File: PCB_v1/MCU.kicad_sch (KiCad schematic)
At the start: 41 parts, among them J8 Conn_ARM_JTAG_SWD_10, J9 Conn_01x03, SW8 SW_Push, SW9 SW_SPDT, U6 STM32F405RGTx, Y1 Crystal

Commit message: adding the crystal
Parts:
- C15, C16, C17, C18, C19, C20, C21, C22, C23, C24, C25, C26, C27, C28, C29: symbol Device:C -> GT_LIbrary:C
- C30, C31: symbol Device:C_Polarized_US -> GT_LIbrary:C_Polarized_US
- D6, D7, D8, D9: symbol Device:LED -> GT_LIbrary:LED
- FB1: symbol Device:FerriteBead -> GT_LIbrary:FerriteBead
- J8: symbol Connector:Conn_ARM_JTAG_SWD_10 -> GT_LIbrary:Conn_ARM_JTAG_SWD_10
- J9: symbol Connector_Generic:Conn_01x03 -> GT_LIbrary:Conn_01x03
- R21, R22, R23: symbol Device:R_US -> GT_LIbrary:R_US
- RN3, RN4: symbol Device:R_Pack04_Split -> GT_LIbrary:R_Pack04_Split
- SW8: symbol Switch:SW_Push -> GT_LIbrary:SW_Push
- SW9: symbol Switch:SW_SPDT -> GT_LIbrary:SW_SPDT
- TP10, TP11, TP12, TP13, TP7, TP8, TP9: symbol Connector:TestPoint -> GT_LIbrary:TestPoint
- U6: symbol MCU_ST_STM32F4:STM32F405RGTx -> GT_LIbrary:STM32F405RGTx
- XTAL1: symbol MC306:MC-306_32.7680K-E3_ROHS -> GT_LIbrary:MC-306_32.7680K-E3_ROHS
- Y1: footprint (none) -> LFXTAL003237Bulk; symbol Device:Crystal -> GT_LIbrary:Crystal

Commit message: before oscilator
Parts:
- XTAL1: footprint Parts_Library:SO4_MC-306_SEC -> SO4_MC-306_SEC
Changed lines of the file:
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@@
 			)
 		)
-		(property "Footprint" "Parts_Library:SO4_MC-306_SEC"
+		(property "Footprint" "SO4_MC-306_SEC"
 			(at 64.77 203.2 0)
 			(effects

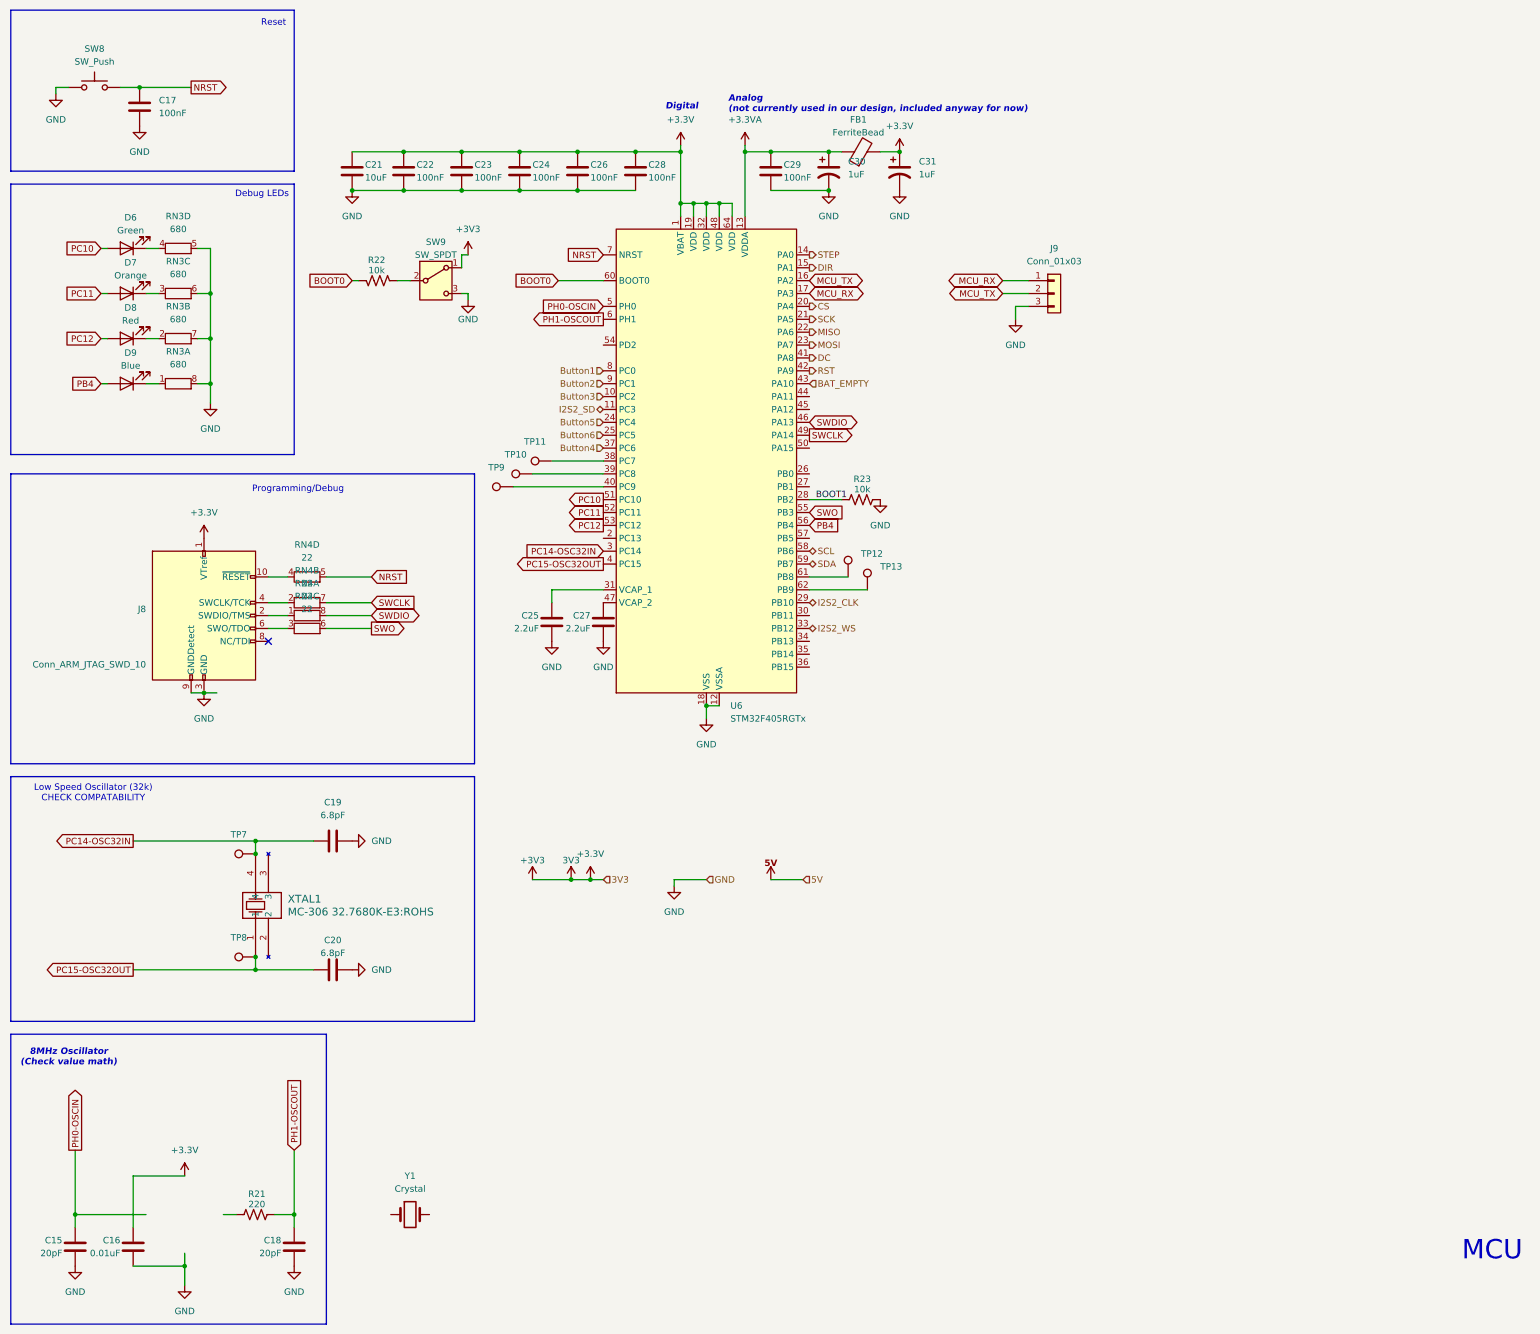
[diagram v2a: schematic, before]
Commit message: added the oscilator
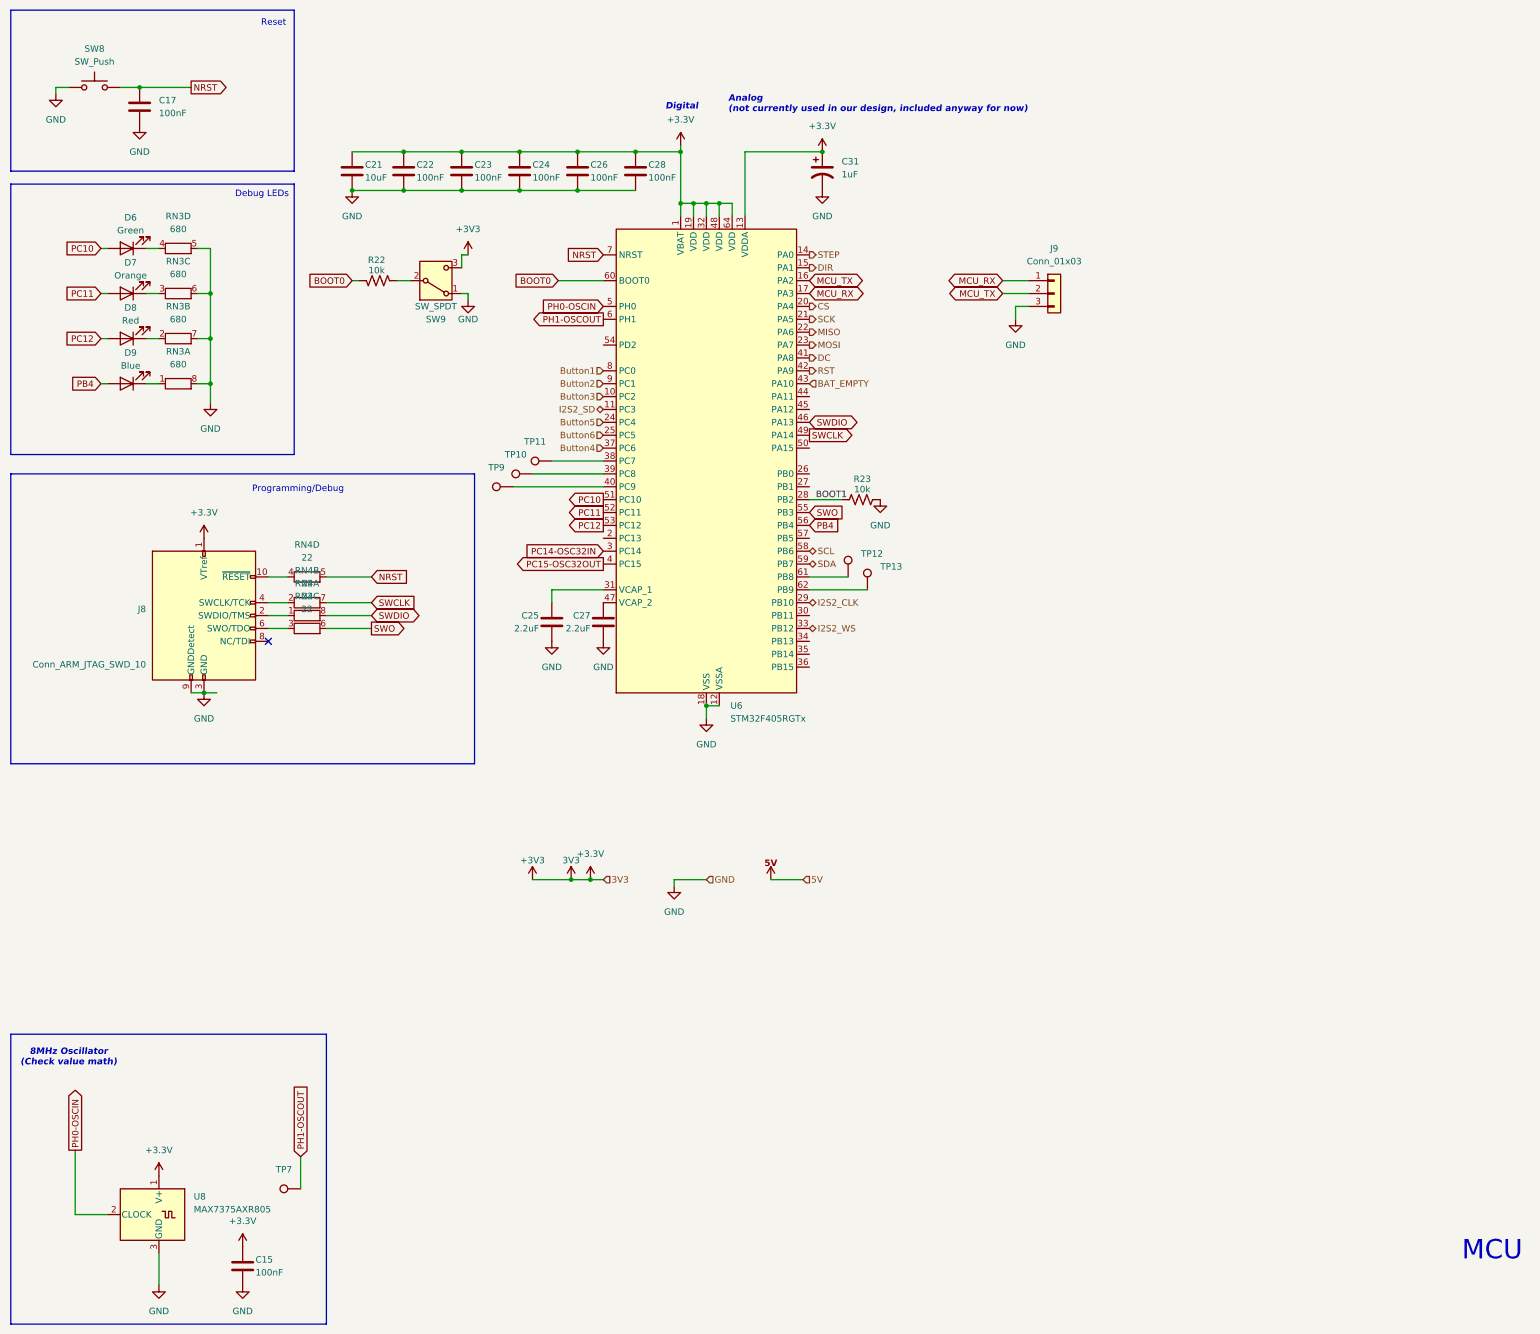
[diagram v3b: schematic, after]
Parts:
- removed C16: 0.01uF, Capacitor_SMD:C_0805_2012Metric, symbol GT_LIbrary:C
- removed C18: 20pF, Capacitor_SMD:C_0805_2012Metric, symbol GT_LIbrary:C
- removed C19, C20: 6.8pF, Capacitor_SMD:C_0805_2012Metric, symbol GT_LIbrary:C
- removed C29: 100nF, Capacitor_SMD:C_0805_2012Metric, symbol GT_LIbrary:C
- removed C30: 1uF, Capacitor_SMD:C_1206_3216Metric_Pad1.33x1.80mm_HandSolder, symbol GT_LIbrary:C_Polarized_US
- removed FB1: FerriteBead, Inductor_SMD:L_0603_1608Metric, symbol GT_LIbrary:FerriteBead
- removed R21: 220, Resistor_SMD:R_0805_2012Metric, symbol GT_LIbrary:R_US
- removed TP8: ~, TestPoint:TestPoint_THTPad_D1.0mm_Drill0.5mm, symbol GT_LIbrary:TestPoint
- removed XTAL1: MC-306 32.7680K-E3:ROHS, SO4_MC-306_SEC, symbol GT_LIbrary:MC-306_32.7680K-E3_ROHS
- removed Y1: Crystal, LFXTAL003237Bulk, symbol GT_LIbrary:Crystal
- added U8: MAX7375AXR805, Package_TO_SOT_SMD:SOT-323_SC-70, symbol Oscillator:MAX7375AXR805
- C15: value 20pF -> 100nF
- D6, D7, D8, D9: footprint LED_SMD:LED_0805_2012Metric_Pad1.15x1.40mm_HandSolder -> LED_0805_2012Metric_Pad1.15x1.40mm_HandSolder
- TP10, TP11, TP12, TP13, TP7, TP9: footprint TestPoint:TestPoint_THTPad_D1.0mm_Drill0.5mm -> TestPoint_THTPad_D0.5mm_Drill0.3mm
- U6: footprint Package_QFP:LQFP-64_10x10mm_P0.5mm -> LQFP-64_10x10mm_P0.5mm
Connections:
- net +3.3VA is gone; now on net +3.3V: U6.13 (VDDA)
- net +3.3V: now also C15.1, SW9.3 (C), U8.1 (V+); no longer SW9.1 (A)
- net GND: now also SW9.1 (A), U8.3 (GND); no longer SW9.3 (C)
- net PC14-OSC32IN: no longer TP7.1
- net PH0-OSCIN: now also U8.2 (CLOCK); no longer C15.1
- net PH1-OSCOUT: now also TP7.1
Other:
- note removed: "Low Speed Oscillator (32k) CHECK COMPATABILITY"
- moved on the sheet: C31

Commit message: push for jtag fix
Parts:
- J8: footprint Connector_PinHeader_2.54mm:PinHeader_2x05_P2.54mm_Vertical -> Connector_IDC:IDC-Header_2x05_P2.54mm_Vertical
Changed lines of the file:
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@@
 	(label "BOOT1"
 		(at 175.26 113.03 0)
-		(fields_autoplaced yes)
 		(effects
 			(font
@@
 		(shape bidirectional)
 		(at 173.99 138.43 0)
-		(fields_autoplaced yes)
 		(effects
 			(font
@@
 		(shape input)
 		(at 172.72 187.96 0)
-		(fields_autoplaced yes)
 		(effects
 			(font
@@
 		(shape output)
 		(at 173.99 80.01 0)
-		(fields_autoplaced yes)
 		(effects
 			(font
@@
 		(shape bidirectional)
 		(at 173.99 125.73 0)
-		(fields_autoplaced yes)
 		(effects
 			(font
@@
 		(shape output)
 		(at 173.99 85.09 0)
-		(fields_autoplaced yes)
 		(effects
 			(font
@@
 		(shape input)
 		(at 133.35 100.33 180)
-		(fields_autoplaced yes)
 		(effects
 			(font
@@
 		(shape input)
 		(at 173.99 90.17 0)
-		(fields_autoplaced yes)
 		(effects
 			(font
@@
 		(shape output)
 		(at 173.99 87.63 0)
-		(fields_autoplaced yes)
 		(effects
 			(font
@@
 		(shape input)
 		(at 133.35 92.71 180)
-		(fields_autoplaced yes)
 		(effects
 			(font
@@
 		(shape input)
 		(at 133.35 102.87 180)
-		(fields_autoplaced yes)
 		(effects
 			(font
@@
 		(shape input)
 		(at 133.35 97.79 180)
-		(fields_autoplaced yes)
 		(effects
 			(font
@@
 		(shape input)
 		(at 133.35 187.96 0)
-		(fields_autoplaced yes)
 		(effects
 			(font
@@
 		(shape input)
 		(at 133.35 90.17 180)
-		(fields_autoplaced yes)
 		(effects
 			(font
@@
 		(shape input)
 		(at 153.67 187.96 0)
-		(fields_autoplaced yes)
 		(effects
 			(font
@@
 		(shape output)
 		(at 173.99 74.93 0)
-		(fields_autoplaced yes)
 		(effects
 			(font
@@
 		(shape output)
 		(at 173.99 77.47 0)
-		(fields_autoplaced yes)
 		(effects
 			(font
@@
 		(shape output)
 		(at 173.99 64.77 0)
-		(fields_autoplaced yes)
 		(effects
 			(font
@@
 		(shape output)
 		(at 173.99 82.55 0)
-		(fields_autoplaced yes)
 		(effects
 			(font
@@
 		(shape bidirectional)
 		(at 133.35 95.25 180)
-		(fields_autoplaced yes)
 		(effects
 			(font
@@
 		(shape bidirectional)
 		(at 173.99 123.19 0)
-		(fields_autoplaced yes)
 		(effects
 			(font
@@
 		(shape input)
 		(at 133.35 87.63 180)
-		(fields_autoplaced yes)
 		(effects
 			(font
@@
 		(shape bidirectional)
 		(at 173.99 133.35 0)
-		(fields_autoplaced yes)
 		(effects
 			(font
@@
 		(shape output)
 		(at 173.99 67.31 0)
-		(fields_autoplaced yes)
 		(effects
 			(font
@@
 			)
 		)
-		(property "Footprint" "Connector_PinHeader_2.54mm:PinHeader_2x05_P2.54mm_Vertical"
+		(property "Footprint" "Connector_IDC:IDC-Header_2x05_P2.54mm_Vertical"
 			(at 52.832 140.462 0)
 			(effects

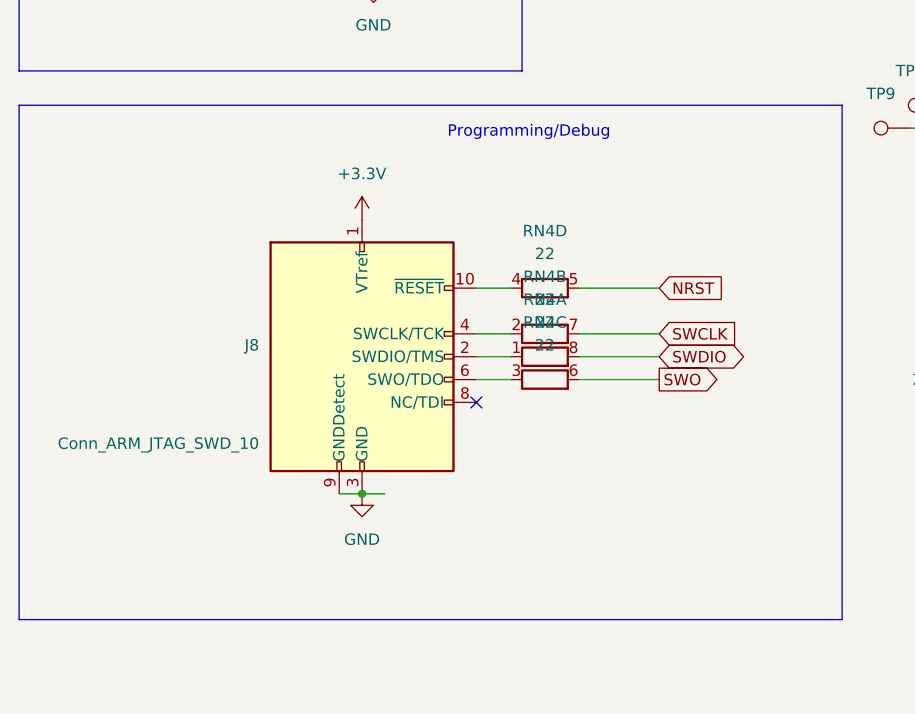
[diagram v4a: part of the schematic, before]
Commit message: Updated debug connection on MCU
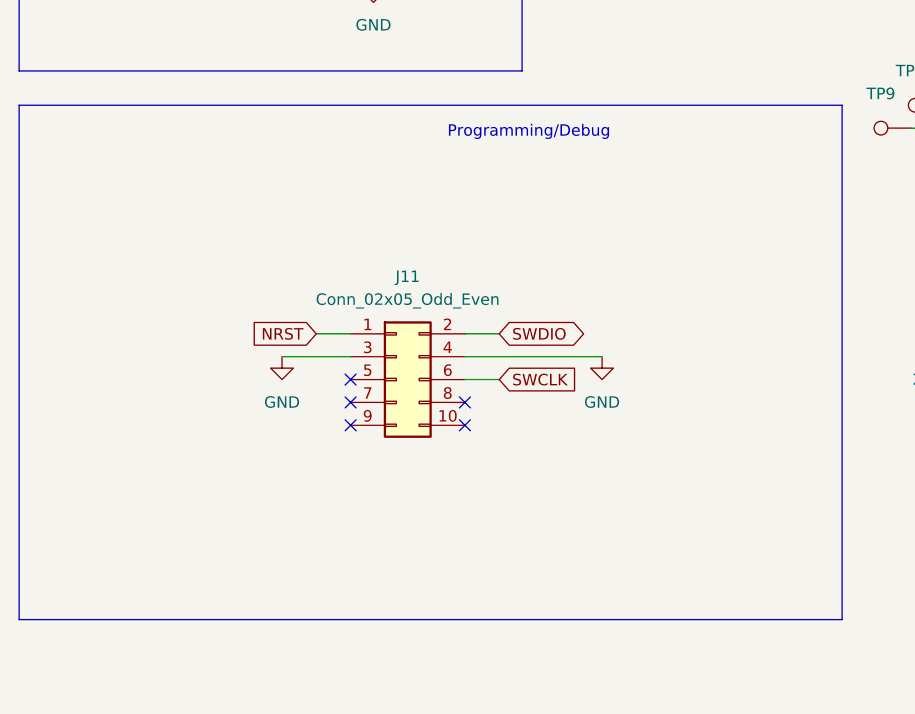
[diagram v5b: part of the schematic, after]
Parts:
- removed J8: Conn_ARM_JTAG_SWD_10, Connector_IDC:IDC-Header_2x05_P2.54mm_Vertical, symbol GT_LIbrary:Conn_ARM_JTAG_SWD_10
- removed RN4: 22, Parts_Library:RESCAXE80P320X160X70-8N, symbol GT_LIbrary:R_Pack04_Split
- added J11: Conn_02x05_Odd_Even, Connector_Harwin:Harwin_LTek-Male_2x05_P2.00mm_Vertical, symbol Connector_Generic:Conn_02x05_Odd_Even
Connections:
- net GND: now also J11.3 (Pin_3), J11.4 (Pin_4)
- net NRST: now also J11.1 (Pin_1)
- net SWCLK: now also J11.6 (Pin_6)
- net SWDIO: now also J11.2 (Pin_2)
- no-connect marks 1 -> 5

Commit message: before major move
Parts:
- added J8: Conn_01x02_Pin, Connector_PinHeader_2.54mm:PinHeader_1x02_P2.54mm_Vertical, symbol Connector:Conn_01x02_Pin
- added R23: 10k, Resistor_SMD:R_0805_2012Metric, symbol GT_LIbrary:R_US
- J9: renamed from J11; footprint Connector_Harwin:Harwin_LTek-Male_2x05_P2.00mm_Vertical -> Connector_IDC:IDC-Header_2x05_P2.54mm_Vertical
- TP10: renamed from TP11; footprint TestPoint_THTPad_D0.5mm_Drill0.3mm -> TestPoint_THTPad_D0.8mm_Drill0.4mm
- TP11: renamed from TP12; footprint TestPoint_THTPad_D0.5mm_Drill0.3mm -> TestPoint_THTPad_D0.8mm_Drill0.4mm
- TP12: renamed from TP13; footprint TestPoint_THTPad_D0.5mm_Drill0.3mm -> TestPoint_THTPad_D0.8mm_Drill0.4mm
- TP7: footprint TestPoint_THTPad_D0.5mm_Drill0.3mm -> TestPoint_THTPad_D0.8mm_Drill0.4mm
- TP8: renamed from TP9; footprint TestPoint_THTPad_D0.5mm_Drill0.3mm -> TestPoint_THTPad_D0.8mm_Drill0.4mm
- TP9: renamed from TP10; footprint TestPoint_THTPad_D0.5mm_Drill0.3mm -> TestPoint_THTPad_D0.8mm_Drill0.4mm
- renumbered C17 to C15, C15 to C16, C21 to C17, C22 to C18, C23 to C19, C24 to C20, C25 to C21, C26 to C22, C27 to C23, C28 to C24, C31 to C25, J9 to J10, R22 to R21, R23 to R22, U8 to U6, U6 to U7
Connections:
- net +3.3V: now also J8.1 (Pin_1), R23.1
- net NRST: now also R23.2
- net at J9.7 (Pin_7): now also J9.8 (Pin_8), J8.2 (Pin_2)
- no-connect marks 5 -> 3

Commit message: Placement done
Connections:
- net MCU_RX: now also J10.2 (Pin_2); no longer J10.1 (Pin_1)
- net MCU_TX: now also J10.1 (Pin_1); no longer J10.2 (Pin_2)
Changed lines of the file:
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@@
-	(wire
-		(pts
-			(xy 212.09 72.39) (xy 217.17 72.39)
-		)
-		(stroke
-			(width 0)
-			(type default)
-		)
-	)
 	(wire
 		(pts
@@
 	(wire
 		(pts
-			(xy 212.09 69.85) (xy 217.17 69.85)
-		)
-		(stroke
-			(width 0)
-			(type default)
-		)
-	)
-	(wire
-		(pts
 			(xy 173.99 130.81) (xy 185.42 130.81)
 		)
@@
 	(wire
 		(pts
+			(xy 214.63 72.39) (xy 217.17 72.39)
+		)
+		(stroke
+			(width 0)
+			(type default)
+		)
+	)
+	(wire
+		(pts
 			(xy 153.67 153.67) (xy 156.21 153.67)
 		)
@@
 	(wire
 		(pts
+			(xy 176.53 138.43) (xy 173.99 138.43)
+		)
+		(stroke
+			(width 0)
+			(type default)
+		)
+	)
+	(wire
+		(pts
 			(xy 69.85 146.05) (xy 49.53 146.05)
 		)
@@
 	(wire
 		(pts
+			(xy 214.63 69.85) (xy 217.17 69.85)
+		)
+		(stroke
+			(width 0)
+			(type default)
+		)
+	)
+	(wire
+		(pts
 			(xy 35.56 63.5) (xy 34.29 63.5)
 		)
@@
 		(pts
 			(xy 53.34 72.39) (xy 55.88 72.39)
+		)
+		(stroke
+			(width 0)
+			(type default)
+		)
+	)
+	(wire
+		(pts
+			(xy 176.53 133.35) (xy 173.99 133.35)
 		)
 		(stroke
@@
 	(global_label "MCU_TX"
 		(shape bidirectional)
-		(at 212.09 72.39 180)
-		(fields_autoplaced yes)
-		(effects
-			(font
-				(size 1.27 1.27)
-			)
-			(justify right)
-		)
-		(property "Intersheetrefs" "${INTERSHEET_REFS}"
-			(at 200.7969 72.39 0)
+		(at 214.63 69.85 180)
+		(fields_autoplaced yes)
+		(effects
+			(font
+				(size 1.27 1.27)
+			)
+			(justify right)
+		)
+		(property "Intersheetrefs" "${INTERSHEET_REFS}"
+			(at 203.3369 69.85 0)
 			(effects
 				(font
@@
 	(global_label "MCU_RX"
 		(shape bidirectional)
-		(at 212.09 69.85 180)
-		(fields_autoplaced yes)
-		(effects
-			(font
-				(size 1.27 1.27)
-			)
-			(justify right)
-		)
-		(property "Intersheetrefs" "${INTERSHEET_REFS}"
-			(at 200.4945 69.85 0)
+		(at 214.63 72.39 180)
+		(fields_autoplaced yes)
+		(effects
+			(font
+				(size 1.27 1.27)
+			)
+			(justify right)
+		)
+		(property "Intersheetrefs" "${INTERSHEET_REFS}"
+			(at 203.0345 72.39 0)
 			(effects
 				(font
@@
 	(hierarchical_label "I2S2_WS"
 		(shape bidirectional)
-		(at 173.99 138.43 0)
+		(at 176.53 138.43 0)
 		(effects
 			(font
@@
 	(hierarchical_label "I2S2_CLK"
 		(shape bidirectional)
-		(at 173.99 133.35 0)
-		(effects
-			(font
+		(at 176.53 133.35 0)
+		(effects
+			(font
